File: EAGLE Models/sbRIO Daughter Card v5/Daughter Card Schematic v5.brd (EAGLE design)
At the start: 101.6 x 81.3 mm, 81 parts, among them IC1 ITS4880R-PAD, Q1 MMBT4403-7-F, Q10 MMBT4403-7-F, Q11 MMBT4401-7-F, Q13 MMBT4401-7-F, Q2 MMBT4403-7-F, Q7 MMBT4403-7-F, Q8 MMBT4403-7-F, Q9 MMBT4401-7-F, U1 MMBT4403-7-F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

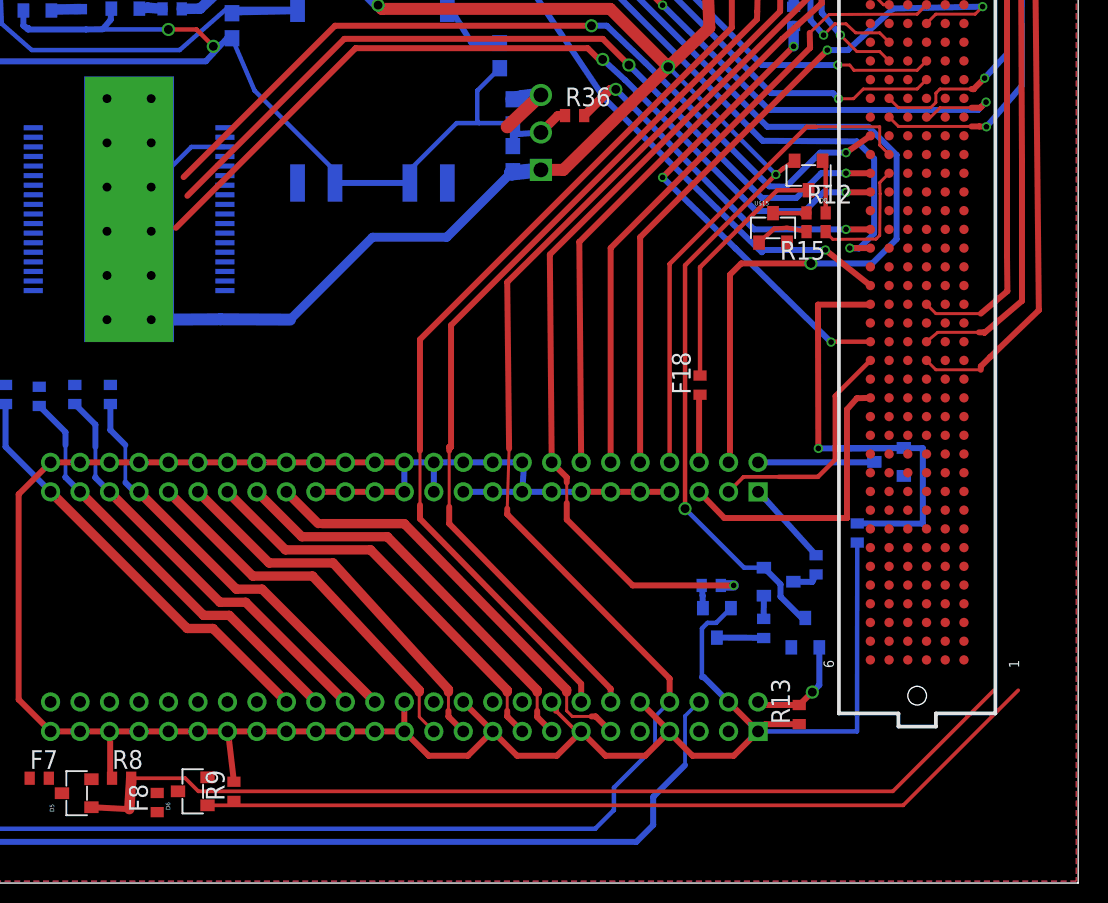
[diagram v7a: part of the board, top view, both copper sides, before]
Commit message: fixed traces that were unnecessary
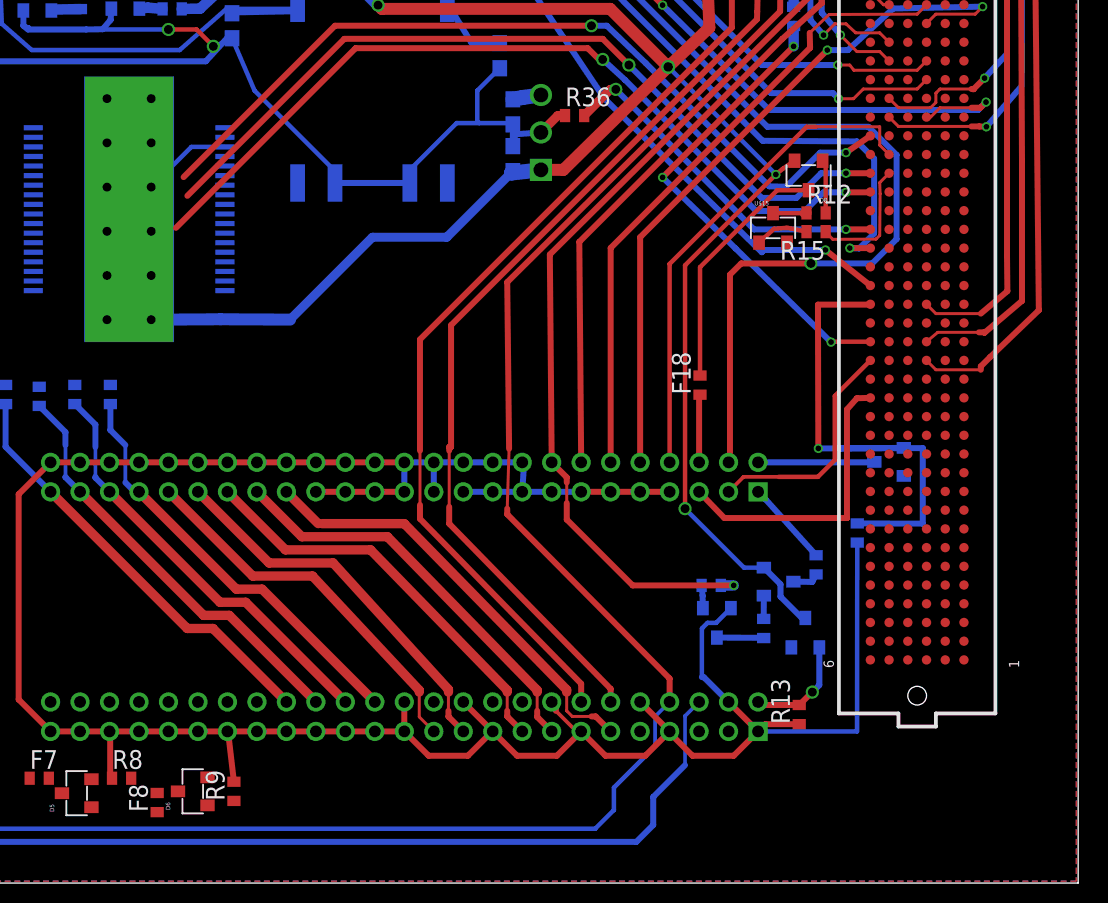
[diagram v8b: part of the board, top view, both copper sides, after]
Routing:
- net N$15: track 66.4 -> 0.00 mm
- net N$16: track 58.2 -> 0.00 mm
- net 5V: track 10.2 -> 7.04 mm
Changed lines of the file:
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@@
 <wire x1="63.246" y1="53.174" x2="63.92" y2="53.301" width="1.016" layer="16"/>
 <wire x1="63.92" y1="53.301" x2="65.151" y2="53.467" width="1.016" layer="16"/>
-<wire x1="65.151" y1="53.467" x2="62.865" y2="51.308" width="0.889" layer="1"/>
-<wire x1="62.865" y1="51.308" x2="25.908" y2="37.846" width="0" layer="19" extent="1-16"/>
 <contactref element="F16" pad="1"/>
 <contactref element="F9" pad="2"/>
 <contactref element="F10" pad="2"/>
-<wire x1="31.481" y1="4.968" x2="26.162" y2="7.874" width="0" layer="19" extent="1-16"/>
-<wire x1="26.162" y1="7.874" x2="25.908" y2="37.846" width="0" layer="19" extent="1-16"/>
 <wire x1="10.145" y1="77.089" x2="10.033" y2="77.089" width="0.3048" layer="16"/>
 <wire x1="10.033" y1="77.089" x2="9.54" y2="77.089" width="0.3048" layer="16"/>
@@
 <wire x1="10.145" y1="78.74" x2="10.033" y2="78.628" width="0.3048" layer="16"/>
 <wire x1="10.033" y1="78.628" x2="10.033" y2="77.089" width="0.3048" layer="16"/>
-<wire x1="10.033" y1="77.089" x2="62.865" y2="51.308" width="0" layer="19" extent="1-16"/>
+<wire x1="10.145" y1="77.089" x2="63.246" y2="53.174" width="0" layer="19" extent="16-16"/>
 </signal>
 <signal name="GND">
@@
 <contactref element="U$3" pad="192"/>
 <contactref element="R8" pad="2"/>
-<wire x1="37.353" y1="7.112" x2="37.226" y2="5.013" width="0.7112" layer="1"/>
-<wire x1="37.226" y1="5.013" x2="34.655" y2="5.146" width="0.4064" layer="1"/>
-<wire x1="37.226" y1="5.013" x2="37.226" y2="5.013" width="0" layer="19" extent="1-16"/>
-<wire x1="37.353" y1="7.112" x2="41.021" y2="7.112" width="0.254" layer="1"/>
-<wire x1="41.021" y1="7.112" x2="41.91" y2="6.223" width="0.254" layer="1"/>
-<wire x1="41.91" y1="6.223" x2="89.027" y2="6.223" width="0.254" layer="1"/>
-<wire x1="89.027" y1="6.223" x2="95.885" y2="13.081" width="0.254" layer="1"/>
-<wire x1="95.885" y1="13.081" x2="87.503" y2="54.5084" width="0" layer="19" extent="1-16"/>
+<wire x1="37.353" y1="7.112" x2="87.503" y2="54.5084" width="0" layer="19" extent="1-1"/>
+<wire x1="34.655" y1="5.146" x2="37.353" y2="7.112" width="0" layer="19" extent="1-1"/>
 </signal>
 <signal name="N$16">
@@
 <contactref element="U$3" pad="180"/>
 <contactref element="R9" pad="1"/>
-<wire x1="42.529" y1="5.273" x2="87.503" y2="51.9684" width="0" layer="19" extent="1-1"/>
-<wire x1="42.529" y1="5.273" x2="89.728" y2="5.273" width="0.254" layer="1"/>
-<wire x1="89.728" y1="5.273" x2="97.536" y2="13.081" width="0.254" layer="1"/>
-<wire x1="97.536" y1="13.081" x2="87.503" y2="51.9684" width="0" layer="19" extent="1-16"/>
+<wire x1="44.323" y1="5.573" x2="87.503" y2="51.9684" width="0" layer="19" extent="1-1"/>
+<wire x1="42.529" y1="5.273" x2="44.323" y2="5.573" width="0" layer="19" extent="1-1"/>
 </signal>
 <signal name="CAN_H">
@@
 <contactref element="F8" pad="1"/>
 <contactref element="ACCUMULATOR_CONN" pad="7"/>
-<wire x1="11.43" y1="13.335" x2="39.116" y2="4.811" width="0" layer="19" extent="16-16"/>
+<wire x1="11.43" y1="13.335" x2="39.116" y2="4.811" width="0" layer="19" extent="1-1"/>
 </signal>
 <signal name="N$14">
